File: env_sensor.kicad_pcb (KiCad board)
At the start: 2 copper layers, 147.9 x 143 mm, 56 parts, among them J1 E Paper, J10 PWMOUT, J11 Reg2, J12 I2C_Source, J13 I2C_2, J14 I2C_3, J15 MH-Z19, J16 ADCs, J17 Conn_01x04_Pin, J2 Reg1, J3 Barrel_Jack, J4 LED_OUTPUT, J5 Conn_01x04_Pin, J6 I2C_1, J6 I2c, J7 USB_C_Receptacle_USB2.0_16P, J9 DEBUG, Q1 NMOS, Q2 NMOS, Q3 NMOS, U1 MH-Z19B, U3 ESP32-S3-WROOM-1, U4 TXB0104PW, U6 TPS2065CDBV, U7 AP7361C-33E, Y1 Crystal

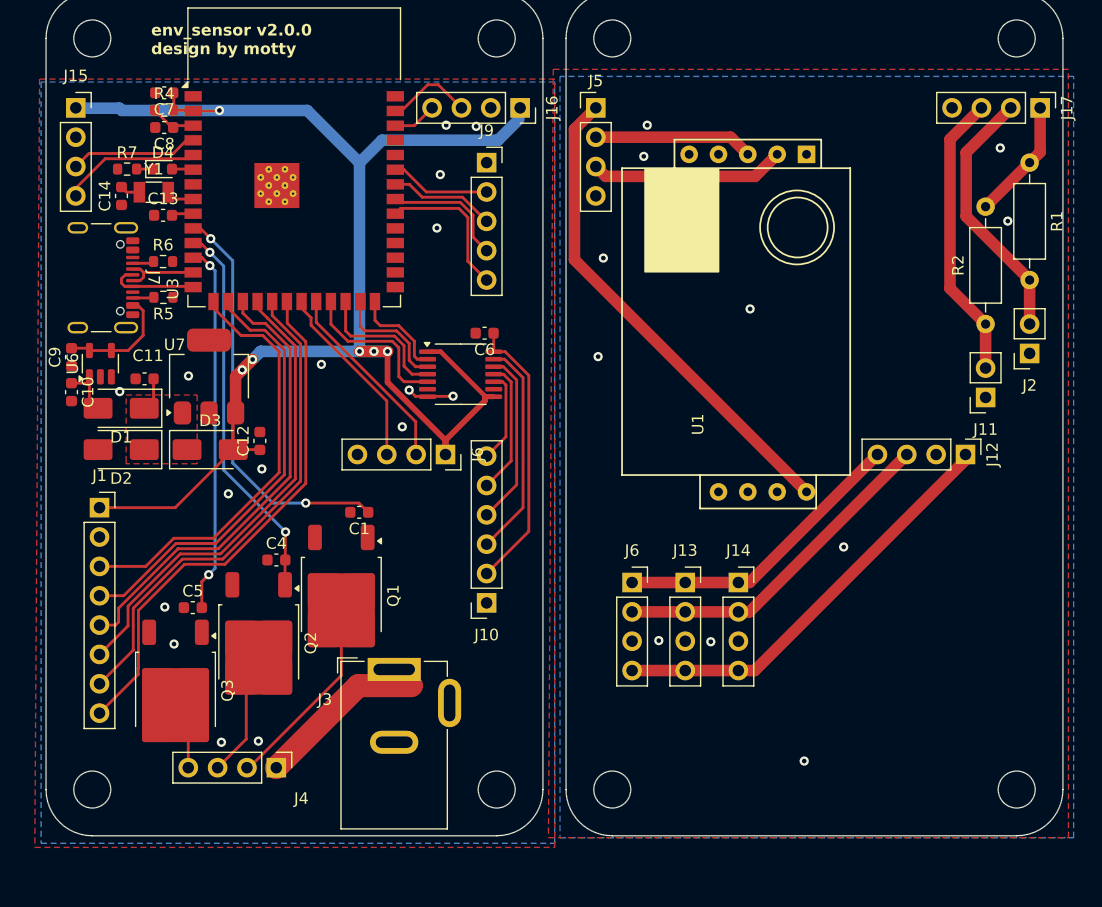
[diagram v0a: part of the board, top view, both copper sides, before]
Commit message: update lib for switch and fix DRCs
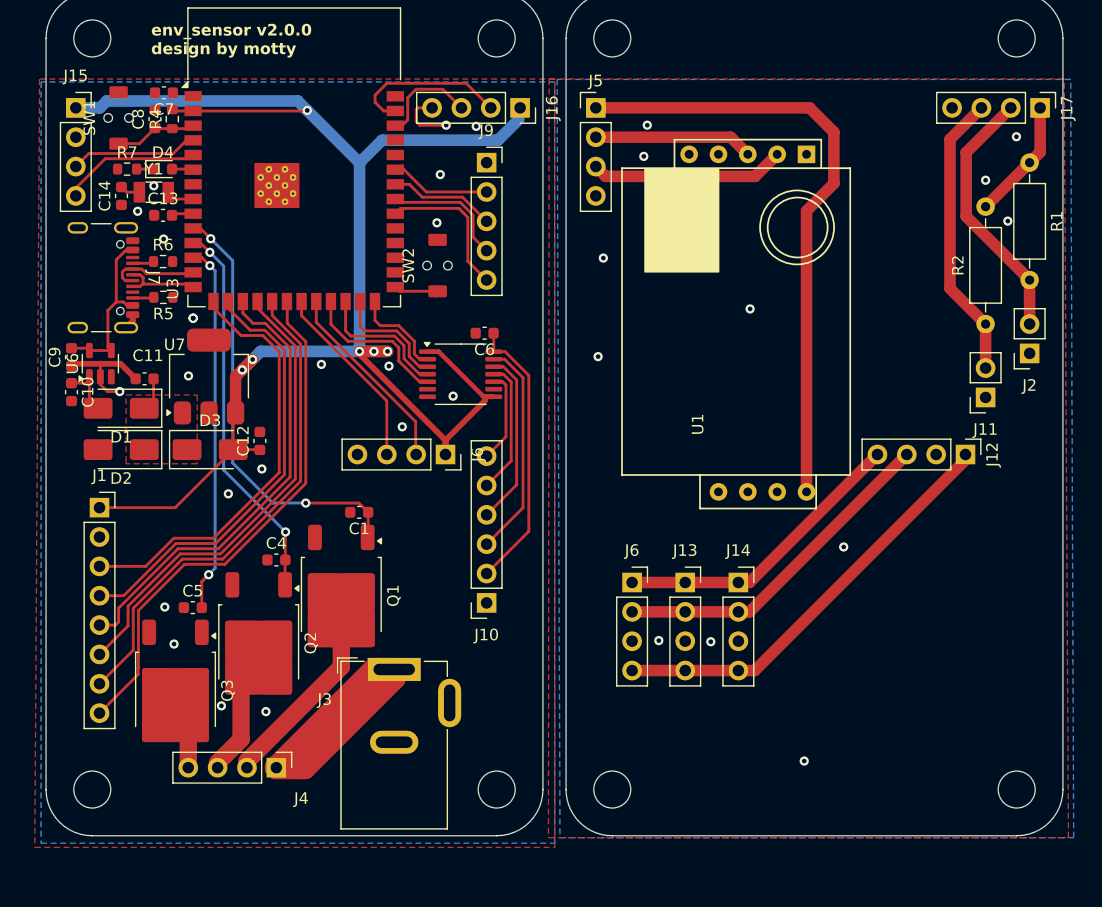
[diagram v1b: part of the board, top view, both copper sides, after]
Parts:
- added SW1: EN, paripalpp_button:TVAF06-A020B-R, F.Cu at (106.3, 51.9)
- added SW2: BOOT, paripalpp_button:TVAF06-A020B-R, F.Cu at (133.9, 64.7)
- moved C8 1.08 mm to (109.4, 52.0), turned to 90 degrees
- moved R4 1.04 mm to (110.9, 52.0), turned to 90 degrees
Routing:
- net v12: track 14.6 -> 27.9 mm
- net GND: track 3.93 -> 16.5 mm, vias 16 -> 21
- net /sensor/v5v: track 42.3 -> 53.6 mm
- net v3v: track 130.0 -> 137.6 mm
- net adc1: track 7.49 -> 14.5 mm
- net Net-(U6-EN): track 10.1 -> 15.1 mm
- net adc2: track 3.82 -> 8.82 mm
- net IO0: track 0.00 -> 4.79 mm
- net EN: track 4.01 -> 7.14 mm
- net LED_C1: track 35.6 -> 37.8 mm
- net IO19: track 6.82 -> 7.93 mm
- net AD3: track 13.8 -> 13.1 mm
- net LED_V2: track 11.0 -> 10.2 mm
- net /sensor/GND: vias 11 -> 12

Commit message: update
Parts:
- added J18: Conn_01x02_Pin, Connector_PinHeader_2.54mm:PinHeader_1x02_P2.54mm_Vertical, F.Cu at (138.1, 100.9)
- added J8: v5_v3, Connector_PinSocket_2.54mm:PinSocket_1x03_P2.54mm_Vertical, F.Cu at (132.9, 93.8)
- J12, J17, J5: moved to B.Cu
- J9: footprint Connector_PinSocket_2.54mm:PinSocket_1x05_P2.54mm_Vertical -> Connector_PinHeader_2.54mm:PinHeader_1x05_P2.54mm_Vertical
- moved J13 26.6 mm to (181.7, 88.7), turned to 180 degrees
- moved C6 21.7 mm to (135.6, 92.1), turned to -90 degrees
- moved J14 18.3 mm to (176.1, 100.7), turned to 90 degrees
- moved J12 11.7 mm to (172.0, 72.1), turned to 180 degrees
- moved J6 11.6 mm to (127.1, 72.1), turned to 0 degrees
- moved SW2 10.0 mm to (138.1, 73.7), turned to 0 degrees
- moved U4 9.83 mm to (131.9, 83.0), turned to -90 degrees
- moved J6 8.81 mm to (148.7, 100.7), turned to 90 degrees
- moved SW1 7.05 mm to (101.9, 57.4), turned to 0 degrees
- moved C8 5.24 mm to (104.6, 54.0)
- moved R4 5.23 mm to (106.1, 54.0)
- moved C7 5.02 mm to (107.6, 54.0), turned to -90 degrees
- moved J11 4.63 mm to (181.5, 71.4)
- moved R2 3.86 mm to (181.5, 65.9)
- moved J2 0.81 mm to (185.1, 71.4)
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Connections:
- net Net-(J10-Pin_2) renamed /VServo
- J15 pad 1: v3v -> VCC
- J15 pad 3: RX(ESP_DOWN) -> TX(ESP_UP)
- J15 pad 4: TX(ESP_UP) -> RX(ESP_DOWN)
- J5 pad 2: /sensor/UART(d2u) -> /sensor/GND
- J5 pad 3: /sensor/UART(u2d) -> /sensor/TX(ESP_DOWN)
- J5 pad 4: /sensor/GND -> /sensor/RX(ESP_UP)
- U1 pad 2: /sensor/UART(u2d) -> /sensor/RX(ESP_UP)
- U1 pad 3: /sensor/UART(d2u) -> /sensor/TX(ESP_DOWN)
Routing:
- net VCC: track 4.01 -> 79.4 mm, vias 0 -> 4
- net v5v: track 0.00 -> 69.2 mm
- net /sensor/SCL: track 29.4 -> 65.8 mm
- net /sensor/SDA: track 25.8 -> 61.1 mm
- net /sensor/v3v: track 36.9 -> 65.8 mm
- net /sensor/UART(u2d): track 16.8 -> 0.00 mm
- net /sensor/UART(d2u): track 13.8 -> 0.00 mm
- net /sensor/v5v: track 53.6 -> 40.8 mm
- net Net-(J10-Pin_3): track 18.9 -> 8.52 mm
- net /sensor/TX(ESP_DOWN): track 0.00 -> 10.1 mm
- net /sensor/RX(ESP_UP): track 0.00 -> 10.1 mm
- net EN: track 7.14 -> 15.5 mm, vias 0 -> 2
- net Net-(J10-Pin_4): track 15.2 -> 7.46 mm
- net SCL: track 17.0 -> 10.0 mm
- net /VServo: track 24.2 -> 17.2 mm
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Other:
- board text added: "VCC GND MOSI SCLK CS DC RST BL"
- board text added: "env_sensor v3.0.0 design by motty LazyStance"
- board text removed: "${REFERENCE}"
- board text removed: "env_sensor v2.0.0 design by motty"

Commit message: ok
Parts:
- J6: value I2c -> ADCs
- J7: footprint Connector_USB:USB_C_Receptacle_GCT_USB4105-xx-A_16P_TopMnt_Horizontal -> Connector_USB:USB_C_Receptacle_GCT_USB4085
- moved J18 39.0 mm to (104.6, 81.1)
- moved C12 8.21 mm to (113.8, 86.6)
- moved C11 4.20 mm to (112.7, 74.2), turned to 90 degrees
- moved U6 4.19 mm to (108.9, 73.6)
- moved J7 3.86 mm to (106.2, 62.7)
- moved D2 3.49 mm to (109.9, 81.1)
- moved C10 3.46 mm to (105.6, 74.8), turned to 180 degrees
- moved D1 3.44 mm to (109.9, 77.5)
- moved C9 3.36 mm to (105.6, 72.5), turned to 0 degrees
- moved J22 3.15 mm to (151.9, 100.6)
- moved U7 3.15 mm to (117.2, 74.9)
- moved D3 2.93 mm to (117.1, 81.1)
- renumbered J6 to J22
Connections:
- J15 pad 3: TX(ESP_UP) -> RX(ESP_DOWN)
- J15 pad 4: RX(ESP_DOWN) -> TX(ESP_UP)
- J6 pad 2: SCL -> GND
- J6 pad 3: SDA -> SCL
- J6 pad 4: GND -> SDA
- U3 pad 4: RX(ESP_DOWN) -> TX(ESP_UP)
- U3 pad 5: TX(ESP_UP) -> RX(ESP_DOWN)
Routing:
- net v5v: track 69.2 -> 3.33 mm
- net Net-(U6-EN): track 14.7 -> 27.1 mm
- net GND: track 13.4 -> 2.11 mm, vias 30 -> 31
- net Net-(J7-CC2): track 1.87 -> 10.5 mm, vias 0 -> 1
- net VCC: track 79.4 -> 73.4 mm
- net v3v: track 139.0 -> 133.6 mm
- net /sensor/SDA: track 61.1 -> 57.9 mm
- net /sensor/SCL: track 65.8 -> 62.7 mm
- net /sensor/v3v: track 65.8 -> 62.7 mm
- net SDA: track 11.4 -> 14.2 mm
- net TX(ESP_UP): track 7.89 -> 5.12 mm
- net RX(ESP_DOWN): track 5.12 -> 7.89 mm
- net SCL: track 10.0 -> 12.1 mm
- net IO20: track 10.1 -> 11.9 mm, vias 2 -> 1
- net SPI_SCLK: track 38.1 -> 39.8 mm
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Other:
- board text added: "3.3V GND"
- board text added: "3.3V GND SCL SDA"
- board text added: "ADC1_CH0 ADC1_CH1"
- board text added: "GND TMS TDI TD0 TCK"

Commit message: update
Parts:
- removed J13: I2C_2, Connector_PinSocket_2.54mm:PinSocket_1x04_P2.54mm_Vertical
- removed J14: I2C_3, Connector_PinSocket_2.54mm:PinSocket_1x04_P2.54mm_Vertical
- removed J22: I2C_1, Connector_PinSocket_2.54mm:PinSocket_1x04_P2.54mm_Vertical
- added ?: , , F.Cu at (160.2, 88.4)
- added ?: , , F.Cu at (157.6, 98.6)
- added ?: , , F.Cu at (152.5, 101.1)
- added ?: , , F.Cu at (183.0, 96.0)
- added ?: , , F.Cu at (185.6, 91.0)
- added ?: , , F.Cu at (150.0, 96.0)
- added ?: , , F.Cu at (175.4, 96.0)
- added ?: , , F.Cu at (183.0, 93.5)
- added ?: , , F.Cu at (160.2, 103.7)
- added ?: , , F.Cu at (155.1, 106.2)
- added ?: , , F.Cu at (155.1, 96.0)
- added ?: , , F.Cu at (167.8, 103.7)
- added ?: , , F.Cu at (152.5, 106.2)
- added ?: , , F.Cu at (167.8, 98.6)
- added ?: , , F.Cu at (170.3, 111.3)
- added ?: , , F.Cu at (175.4, 106.2)
- added ?: , , F.Cu at (165.2, 106.2)
- added ?: , , F.Cu at (183.0, 101.1)
- added ?: , , F.Cu at (170.3, 96.0)
- added ?: , , F.Cu at (177.9, 91.0)
- added ?: , , F.Cu at (150.0, 103.7)
- added ?: , , F.Cu at (177.9, 111.3)
- added ?: , , F.Cu at (185.6, 98.6)
- added ?: , , F.Cu at (162.7, 91.0)
- added ?: , , F.Cu at (172.8, 96.0)
- added ?: , , F.Cu at (172.8, 91.0)
- added ?: , , F.Cu at (180.5, 106.2)
- added ?: , , F.Cu at (147.4, 98.6)
- added ?: , , F.Cu at (155.1, 98.6)
- added ?: , , F.Cu at (162.7, 85.9)
- added ?: , , F.Cu at (180.5, 91.0)
- added ?: , , F.Cu at (185.6, 96.0)
- added ?: , , F.Cu at (170.3, 108.7)
- added ?: , , F.Cu at (167.8, 106.2)
- added ?: , , F.Cu at (162.7, 98.6)
- added ?: , , F.Cu at (180.5, 103.7)
- added ?: , , F.Cu at (165.2, 88.4)
- added ?: , , F.Cu at (160.2, 96.0)
- added ?: , , F.Cu at (177.9, 106.2)
- added ?: , , F.Cu at (162.7, 101.1)
- added ?: , , F.Cu at (165.2, 108.7)
- added ?: , , F.Cu at (183.0, 98.6)
- added ?: , , F.Cu at (170.3, 101.1)
- added ?: , , F.Cu at (177.9, 103.7)
- added ?: , , F.Cu at (150.0, 88.4)
- added ?: , , F.Cu at (183.0, 85.9)
- added ?: , , F.Cu at (162.7, 106.2)
- added ?: , , F.Cu at (155.1, 103.7)
- added ?: , , F.Cu at (183.0, 91.0)
- added ?: , , F.Cu at (157.6, 101.1)
- added ?: , , F.Cu at (150.0, 98.6)
- added ?: , , F.Cu at (162.7, 108.7)
- added ?: , , F.Cu at (167.8, 111.3)
- added ?: , , F.Cu at (155.1, 93.5)
- added ?: , , F.Cu at (162.7, 103.7)
- added ?: , , F.Cu at (175.4, 103.7)
- added ?: , , F.Cu at (167.8, 108.7)
- added ?: , , F.Cu at (147.4, 85.9)
- added ?: , , F.Cu at (180.5, 88.4)
- added ?: , , F.Cu at (185.6, 85.9)
- added ?: , , F.Cu at (165.2, 93.5)
- added ?: , , F.Cu at (170.3, 93.5)
- added ?: , , F.Cu at (177.9, 85.9)
- added ?: , , F.Cu at (152.5, 93.5)
- added ?: , , F.Cu at (155.1, 88.4)
- added ?: , , F.Cu at (167.8, 85.9)
- added ?: , , F.Cu at (160.2, 101.1)
- added ?: , , F.Cu at (177.9, 93.5)
- added ?: , , F.Cu at (165.2, 101.1)
- added ?: , , F.Cu at (165.2, 96.0)
- added ?: , , F.Cu at (150.0, 91.0)
- added ?: , , F.Cu at (175.4, 88.4)
- added ?: , , F.Cu at (147.4, 96.0)
- added ?: , , F.Cu at (160.2, 106.2)
- added ?: , , F.Cu at (147.4, 91.0)
- added ?: , , F.Cu at (157.6, 93.5)
- added ?: , , F.Cu at (183.0, 103.7)
- added ?: , , F.Cu at (170.3, 106.2)
- added ?: , , F.Cu at (152.5, 88.4)
- added ?: , , F.Cu at (167.8, 91.0)
- added ?: , , F.Cu at (157.6, 96.0)
- added ?: , , F.Cu at (175.4, 111.3)
- added ?: , , F.Cu at (155.1, 101.1)
- added ?: , , F.Cu at (175.4, 91.0)
- added ?: , , F.Cu at (170.3, 98.6)
- added ?: , , F.Cu at (160.2, 85.9)
- added ?: , , F.Cu at (177.9, 108.7)
- added ?: , , F.Cu at (172.8, 98.6)
- added ?: , , F.Cu at (167.8, 96.0)
- added ?: , , F.Cu at (175.4, 98.6)
- added ?: , , F.Cu at (152.5, 96.0)
- added ?: , , F.Cu at (172.8, 108.7)
- added ?: , , F.Cu at (177.9, 98.6)
- added ?: , , F.Cu at (172.8, 103.7)
- added ?: , , F.Cu at (170.3, 88.4)
- added ?: , , F.Cu at (162.7, 96.0)
- added ?: , , F.Cu at (165.2, 91.0)
- added ?: , , F.Cu at (155.1, 91.0)
- added ?: , , F.Cu at (185.6, 88.4)
- added ?: , , F.Cu at (172.8, 85.9)
- added ?: , , F.Cu at (185.6, 101.1)
- added ?: , , F.Cu at (157.6, 88.4)
- added ?: , , F.Cu at (185.6, 103.7)
- added ?: , , F.Cu at (165.2, 85.9)
- added ?: , , F.Cu at (157.6, 108.7)
- added ?: , , F.Cu at (183.0, 88.4)
- added ?: , , F.Cu at (162.7, 93.5)
- added ?: , , F.Cu at (167.8, 88.4)
- added ?: , , F.Cu at (180.5, 96.0)
- added ?: , , F.Cu at (150.0, 85.9)
- added ?: , , F.Cu at (152.5, 98.6)
- added ?: , , F.Cu at (175.4, 93.5)
- added ?: , , F.Cu at (175.4, 85.9)
- added ?: , , F.Cu at (157.6, 91.0)
- added ?: , , F.Cu at (155.1, 108.7)
- added ?: , , F.Cu at (160.2, 93.5)
- added ?: , , F.Cu at (177.9, 88.4)
- added ?: , , F.Cu at (180.5, 101.1)
- added ?: , , F.Cu at (165.2, 98.6)
- added ?: , , F.Cu at (165.2, 111.3)
- added ?: , , F.Cu at (147.4, 103.7)
- added ?: , , F.Cu at (180.5, 93.5)
- added ?: , , F.Cu at (172.8, 88.4)
- added ?: , , F.Cu at (172.8, 106.2)
- added ?: , , F.Cu at (152.5, 85.9)
- added ?: , , F.Cu at (150.0, 93.5)
- added ?: , , F.Cu at (170.3, 103.7)
- added ?: , , F.Cu at (160.2, 108.7)
- added ?: , , F.Cu at (170.3, 85.9)
- added ?: , , F.Cu at (185.6, 93.5)
- added ?: , , F.Cu at (175.4, 101.1)
- added ?: , , F.Cu at (152.5, 91.0)
- added ?: , , F.Cu at (165.2, 103.7)
- added ?: , , F.Cu at (160.2, 98.6)
- added ?: , , F.Cu at (157.6, 85.9)
- added ?: , , F.Cu at (150.0, 101.1)
- added ?: , , F.Cu at (167.8, 101.1)
- added ?: , , F.Cu at (180.5, 98.6)
- added ?: , , F.Cu at (155.1, 85.9)
- added ?: , , F.Cu at (175.4, 108.7)
- added ?: , , F.Cu at (172.8, 101.1)
- added ?: , , F.Cu at (157.6, 111.3)
- added ?: , , F.Cu at (157.6, 106.2)
- added ?: , , F.Cu at (157.6, 103.7)
- added ?: , , F.Cu at (167.8, 93.5)
- added ?: , , F.Cu at (160.2, 111.3)
- added ?: , , F.Cu at (162.7, 88.4)
- added ?: , , F.Cu at (177.9, 96.0)
- added ?: , , F.Cu at (147.4, 88.4)
- added ?: , , F.Cu at (147.4, 93.5)
- added ?: , , F.Cu at (160.2, 91.0)
- added ?: , , F.Cu at (147.4, 101.1)
- added ?: , , F.Cu at (152.5, 103.7)
- added ?: , , F.Cu at (177.9, 101.1)
- added ?: , , F.Cu at (170.3, 91.0)
- added ?: , , F.Cu at (155.1, 111.3)
- added ?: , , F.Cu at (172.8, 111.3)
- added ?: , , F.Cu at (180.5, 85.9)
- added ?: , , F.Cu at (162.7, 111.3)
- added ?: , , F.Cu at (172.8, 93.5)
- R1, R2: value 1k -> ~
- moved U1 4.55 mm to (147.4, 53.8)
- moved C12 2.10 mm to (114.1, 84.5)
- moved R5 1.81 mm to (109.9, 69.2)
- moved SW1 0.71 mm to (101.9, 56.7)
- moved C7 0.08 mm to (107.5, 54.0)
- moved R4 0.08 mm to (106.0, 54.0)
- moved C8 0.08 mm to (104.5, 54.0)
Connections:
- net Net-(U6-EN) renamed /U6_OUT
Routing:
- net /sensor/SCL: track 62.7 -> 0.00 mm
- net /sensor/v3v: track 62.7 -> 0.00 mm
- net /sensor/SDA: track 57.9 -> 0.00 mm
- net /U6_OUT: track 27.1 -> 15.1 mm
- net /sensor/RX(ESP_UP): track 10.1 -> 5.35 mm
- net /sensor/TX(ESP_DOWN): track 10.1 -> 5.35 mm
- net IO19: track 12.8 -> 8.71 mm, vias 2 -> 1
- net VCC: track 73.4 -> 70.1 mm, vias 4 -> 3
- net IO20: track 11.9 -> 8.78 mm
- net v3v: track 133.6 -> 130.6 mm, vias 7 -> 8
- net adc1: track 13.0 -> 10.4 mm, vias 1 -> 0
- net DEBUG_TCK: track 12.9 -> 10.3 mm
- net /sensor/v5v: track 40.8 -> 38.3 mm
- net Net-(J7-CC2): track 10.5 -> 8.91 mm
- net DEBUG_TDO: track 10.9 -> 9.75 mm
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- added copper zone on F.Cu, net /U6_OUT
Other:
- outline, holes or cut-outs redrawn
- board text removed: "3.3V GND SCL SDA"

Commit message: update
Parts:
- removed ? (x160): , 
- removed REF** (x8): MountingHole_3.2mm_M3, MountingHole:MountingHole_3.2mm_M3
- moved R6 2.63 mm to (108.1, 62.6), turned to 90 degrees
- moved J12 1.39 mm to (172.8, 73.2)
- moved J6 1.28 mm to (127.8, 73.1)
- moved U4 0.92 mm to (132.8, 83.0)
- moved R5 0.22 mm to (109.7, 69.3)
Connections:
- net IO19 renamed USB_D-
- net IO20 renamed USB_D+
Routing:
- net /U6_OUT: track 15.1 -> 19.5 mm
- net GND: track 2.13 -> 0.12 mm, vias 37 -> 32
- net LED_V3: track 5.87 -> 4.31 mm
- net LED_V2: track 10.2 -> 8.69 mm
- net SCL: track 12.1 -> 13.4 mm
- net USB_D+: track 8.78 -> 10.0 mm, vias 1 -> 0
- net SDA: track 14.2 -> 15.4 mm
- net Net-(J7-CC2): track 8.91 -> 9.98 mm
- net Net-(J7-CC1): track 3.34 -> 2.27 mm, vias 1 -> 0
- net Net-(J10-Pin_5): track 7.63 -> 6.66 mm
- net Net-(J10-Pin_6): track 9.25 -> 8.35 mm
- net Net-(J10-Pin_3): track 8.52 -> 7.70 mm
- net v3v: track 130.6 -> 129.8 mm
- net adc1: track 10.4 -> 9.68 mm
- net Net-(J10-Pin_4): track 7.46 -> 6.81 mm
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- added copper zone on F.Cu, net /VServo

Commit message: update
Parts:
- removed D4: POWER, LED_SMD:LED_0603_1608Metric
- removed J12: I2C_Source, Connector_PinHeader_2.54mm:PinHeader_1x04_P2.54mm_Vertical
- removed R7: 1k, Resistor_SMD:R_0603_1608Metric
- added ?: ThroughHole1x01_P2.54mm, env-sensor:ThroughHole1x01_P2.54mm, F.Cu at (177.9, 78.2)
- added ?: ThroughHole1x01_P2.54mm, env-sensor:ThroughHole1x01_P2.54mm, F.Cu at (150.0, 103.7)
- added ?: ThroughHole1x01_P2.54mm, env-sensor:ThroughHole1x01_P2.54mm, F.Cu at (167.8, 80.8)
- added ?: ThroughHole1x01_P2.54mm, env-sensor:ThroughHole1x01_P2.54mm, F.Cu at (162.7, 101.1)
- added ?: ThroughHole1x01_P2.54mm, env-sensor:ThroughHole1x01_P2.54mm, F.Cu at (180.5, 103.7)
- added ?: , , F.Cu at (155.1, 96.0)
- added ?: ThroughHole1x01_P2.54mm, env-sensor:ThroughHole1x01_P2.54mm, F.Cu at (167.8, 101.1)
- added ?: ThroughHole1x01_P2.54mm, env-sensor:ThroughHole1x01_P2.54mm, F.Cu at (157.6, 98.6)
- added ?: ThroughHole1x01_P2.54mm, env-sensor:ThroughHole1x01_P2.54mm, F.Cu at (177.9, 85.9)
- added ?: ThroughHole1x01_P2.54mm, env-sensor:ThroughHole1x01_P2.54mm, F.Cu at (165.2, 88.4)
- added ?: ThroughHole1x01_P2.54mm, env-sensor:ThroughHole1x01_P2.54mm, F.Cu at (185.6, 83.3)
- added ?: ThroughHole1x01_P2.54mm, env-sensor:ThroughHole1x01_P2.54mm, F.Cu at (155.1, 111.3)
- added ?: ThroughHole1x01_P2.54mm, env-sensor:ThroughHole1x01_P2.54mm, F.Cu at (175.4, 106.2)
- added ?: ThroughHole1x01_P2.54mm, env-sensor:ThroughHole1x01_P2.54mm, F.Cu at (162.7, 103.7)
- added ?: ThroughHole1x01_P2.54mm, env-sensor:ThroughHole1x01_P2.54mm, F.Cu at (150.0, 93.5)
- added ?: ThroughHole1x01_P2.54mm, env-sensor:ThroughHole1x01_P2.54mm, F.Cu at (175.4, 96.0)
- added ?: ThroughHole1x01_P2.54mm, env-sensor:ThroughHole1x01_P2.54mm, F.Cu at (150.0, 91.0)
- added ?: ThroughHole1x01_P2.54mm, env-sensor:ThroughHole1x01_P2.54mm, F.Cu at (180.5, 96.0)
- added ?: ThroughHole1x01_P2.54mm, env-sensor:ThroughHole1x01_P2.54mm, F.Cu at (152.5, 91.0)
- added ?: ThroughHole1x01_P2.54mm, env-sensor:ThroughHole1x01_P2.54mm, F.Cu at (177.9, 93.5)
- added ?: ThroughHole1x01_P2.54mm, env-sensor:ThroughHole1x01_P2.54mm, F.Cu at (170.3, 91.0)
- added ?: ThroughHole1x01_P2.54mm, env-sensor:ThroughHole1x01_P2.54mm, F.Cu at (185.6, 101.1)
- added ?: ThroughHole1x01_P2.54mm, env-sensor:ThroughHole1x01_P2.54mm, F.Cu at (170.3, 70.6)
- added ?: ThroughHole1x01_P2.54mm, env-sensor:ThroughHole1x01_P2.54mm, F.Cu at (147.4, 91.0)
- added ?: ThroughHole1x01_P2.54mm, env-sensor:ThroughHole1x01_P2.54mm, F.Cu at (167.8, 98.6)
- added ?: ThroughHole1x01_P2.54mm, env-sensor:ThroughHole1x01_P2.54mm, F.Cu at (165.2, 106.2)
- added ?: ThroughHole1x01_P2.54mm, env-sensor:ThroughHole1x01_P2.54mm, F.Cu at (183.0, 88.4)
- added ?: ThroughHole1x01_P2.54mm, env-sensor:ThroughHole1x01_P2.54mm, F.Cu at (183.0, 83.3)
- added ?: ThroughHole1x01_P2.54mm, env-sensor:ThroughHole1x01_P2.54mm, F.Cu at (172.8, 103.7)
- added ?: ThroughHole1x01_P2.54mm, env-sensor:ThroughHole1x01_P2.54mm, F.Cu at (152.5, 88.4)
- added ?: ThroughHole1x01_P2.54mm, env-sensor:ThroughHole1x01_P2.54mm, F.Cu at (165.2, 91.0)
- added ?: ThroughHole1x01_P2.54mm, env-sensor:ThroughHole1x01_P2.54mm, F.Cu at (172.8, 70.6)
- added ?: ThroughHole1x01_P2.54mm, env-sensor:ThroughHole1x01_P2.54mm, F.Cu at (180.5, 85.9)
- added ?: ThroughHole1x01_P2.54mm, env-sensor:ThroughHole1x01_P2.54mm, F.Cu at (147.4, 88.4)
- added ?: ThroughHole1x01_P2.54mm, env-sensor:ThroughHole1x01_P2.54mm, F.Cu at (175.4, 93.5)
- added ?: ThroughHole1x01_P2.54mm, env-sensor:ThroughHole1x01_P2.54mm, F.Cu at (183.0, 96.0)
- added ?: ThroughHole1x01_P2.54mm, env-sensor:ThroughHole1x01_P2.54mm, F.Cu at (160.2, 88.4)
- added ?: ThroughHole1x01_P2.54mm, env-sensor:ThroughHole1x01_P2.54mm, F.Cu at (172.8, 96.0)
- added ?: ThroughHole1x01_P2.54mm, env-sensor:ThroughHole1x01_P2.54mm, F.Cu at (167.8, 103.7)
- added ?: ThroughHole1x01_P2.54mm, env-sensor:ThroughHole1x01_P2.54mm, F.Cu at (152.5, 93.5)
- added ?: ThroughHole1x01_P2.54mm, env-sensor:ThroughHole1x01_P2.54mm, F.Cu at (147.4, 93.5)
- added ?: ThroughHole1x01_P2.54mm, env-sensor:ThroughHole1x01_P2.54mm, F.Cu at (172.8, 106.2)
- added ?: ThroughHole1x01_P2.54mm, env-sensor:ThroughHole1x01_P2.54mm, F.Cu at (172.8, 108.7)
- added ?: ThroughHole1x01_P2.54mm, env-sensor:ThroughHole1x01_P2.54mm, F.Cu at (183.0, 101.1)
- added ?: , , F.Cu at (155.1, 98.6)
- added ?: ThroughHole1x01_P2.54mm, env-sensor:ThroughHole1x01_P2.54mm, F.Cu at (165.2, 98.6)
- added ?: ThroughHole1x01_P2.54mm, env-sensor:ThroughHole1x01_P2.54mm, F.Cu at (167.8, 88.4)
- added ?: ThroughHole1x01_P2.54mm, env-sensor:ThroughHole1x01_P2.54mm, F.Cu at (170.3, 88.4)
- added ?: ThroughHole1x01_P2.54mm, env-sensor:ThroughHole1x01_P2.54mm, F.Cu at (170.3, 101.1)
- added ?: ThroughHole1x01_P2.54mm, env-sensor:ThroughHole1x01_P2.54mm, F.Cu at (167.8, 75.7)
- added ?: ThroughHole1x01_P2.54mm, env-sensor:ThroughHole1x01_P2.54mm, F.Cu at (157.6, 93.5)
- added ?: ThroughHole1x01_P2.54mm, env-sensor:ThroughHole1x01_P2.54mm, F.Cu at (183.0, 103.7)
- added ?: ThroughHole1x01_P2.54mm, env-sensor:ThroughHole1x01_P2.54mm, F.Cu at (170.3, 98.6)
- added ?: ThroughHole1x01_P2.54mm, env-sensor:ThroughHole1x01_P2.54mm, F.Cu at (165.2, 103.7)
- added ?: , , F.Cu at (155.1, 101.1)
- added ?: ThroughHole1x01_P2.54mm, env-sensor:ThroughHole1x01_P2.54mm, F.Cu at (170.3, 96.0)
- added ?: ThroughHole1x01_P2.54mm, env-sensor:ThroughHole1x01_P2.54mm, F.Cu at (180.5, 91.0)
- added ?: ThroughHole1x01_P2.54mm, env-sensor:ThroughHole1x01_P2.54mm, F.Cu at (160.2, 111.3)
- added ?: ThroughHole1x01_P2.54mm, env-sensor:ThroughHole1x01_P2.54mm, F.Cu at (172.8, 85.9)
- added ?: ThroughHole1x01_P2.54mm, env-sensor:ThroughHole1x01_P2.54mm, F.Cu at (157.6, 96.0)
- added ?: ThroughHole1x01_P2.54mm, env-sensor:ThroughHole1x01_P2.54mm, F.Cu at (167.8, 91.0)
- added ?: ThroughHole1x01_P2.54mm, env-sensor:ThroughHole1x01_P2.54mm, F.Cu at (177.9, 70.6)
- added ?: ThroughHole1x01_P2.54mm, env-sensor:ThroughHole1x01_P2.54mm, F.Cu at (162.7, 96.0)
- added ?: , , F.Cu at (155.1, 91.0)
- added ?: ThroughHole1x01_P2.54mm, env-sensor:ThroughHole1x01_P2.54mm, F.Cu at (185.6, 98.6)
- added ?: ThroughHole1x01_P2.54mm, env-sensor:ThroughHole1x01_P2.54mm, F.Cu at (167.8, 73.2)
- added ?: ThroughHole1x01_P2.54mm, env-sensor:ThroughHole1x01_P2.54mm, F.Cu at (160.2, 101.1)
- added ?: ThroughHole1x01_P2.54mm, env-sensor:ThroughHole1x01_P2.54mm, F.Cu at (150.0, 88.4)
- added ?: ThroughHole1x01_P2.54mm, env-sensor:ThroughHole1x01_P2.54mm, F.Cu at (175.4, 98.6)
- added ?: ThroughHole1x01_P2.54mm, env-sensor:ThroughHole1x01_P2.54mm, F.Cu at (147.4, 101.1)
- added ?: ThroughHole1x01_P2.54mm, env-sensor:ThroughHole1x01_P2.54mm, F.Cu at (170.3, 108.7)
- added ?: ThroughHole1x01_P2.54mm, env-sensor:ThroughHole1x01_P2.54mm, F.Cu at (160.2, 98.6)
- added ?: ThroughHole1x01_P2.54mm, env-sensor:ThroughHole1x01_P2.54mm, F.Cu at (160.2, 96.0)
- added ?: ThroughHole1x01_P2.54mm, env-sensor:ThroughHole1x01_P2.54mm, F.Cu at (162.7, 88.4)
- added ?: ThroughHole1x01_P2.54mm, env-sensor:ThroughHole1x01_P2.54mm, F.Cu at (172.8, 101.1)
- added ?: ThroughHole1x01_P2.54mm, env-sensor:ThroughHole1x01_P2.54mm, F.Cu at (185.6, 91.0)
- added ?: ThroughHole1x01_P2.54mm, env-sensor:ThroughHole1x01_P2.54mm, F.Cu at (177.9, 88.4)
- added ?: ThroughHole1x01_P2.54mm, env-sensor:ThroughHole1x01_P2.54mm, F.Cu at (185.6, 103.7)
- added ?: ThroughHole1x01_P2.54mm, env-sensor:ThroughHole1x01_P2.54mm, F.Cu at (172.8, 98.6)
- added ?: ThroughHole1x01_P2.54mm, env-sensor:ThroughHole1x01_P2.54mm, F.Cu at (147.4, 103.7)
- added ?: , , F.Cu at (162.7, 111.3)
- added ?: ThroughHole1x01_P2.54mm, env-sensor:ThroughHole1x01_P2.54mm, F.Cu at (175.4, 91.0)
- added ?: ThroughHole1x01_P2.54mm, env-sensor:ThroughHole1x01_P2.54mm, F.Cu at (185.6, 96.0)
- added ?: ThroughHole1x01_P2.54mm, env-sensor:ThroughHole1x01_P2.54mm, F.Cu at (167.8, 83.3)
- added ?: ThroughHole1x01_P2.54mm, env-sensor:ThroughHole1x01_P2.54mm, F.Cu at (157.6, 91.0)
- added ?: ThroughHole1x01_P2.54mm, env-sensor:ThroughHole1x01_P2.54mm, F.Cu at (177.9, 96.0)
- added ?: ThroughHole1x01_P2.54mm, env-sensor:ThroughHole1x01_P2.54mm, F.Cu at (177.9, 73.2)
- added ?: ThroughHole1x01_P2.54mm, env-sensor:ThroughHole1x01_P2.54mm, F.Cu at (185.6, 85.9)
- added ?: ThroughHole1x01_P2.54mm, env-sensor:ThroughHole1x01_P2.54mm, F.Cu at (147.4, 96.0)
- added ?: ThroughHole1x01_P2.54mm, env-sensor:ThroughHole1x01_P2.54mm, F.Cu at (175.4, 83.3)
- added ?: , , F.Cu at (155.1, 88.4)
- added ?: ThroughHole1x01_P2.54mm, env-sensor:ThroughHole1x01_P2.54mm, F.Cu at (177.9, 108.7)
- added ?: ThroughHole1x01_P2.54mm, env-sensor:ThroughHole1x01_P2.54mm, F.Cu at (165.2, 101.1)
- added ?: ThroughHole1x01_P2.54mm, env-sensor:ThroughHole1x01_P2.54mm, F.Cu at (147.4, 98.6)
- added ?: ThroughHole1x01_P2.54mm, env-sensor:ThroughHole1x01_P2.54mm, F.Cu at (172.8, 93.5)
- added ?: , , F.Cu at (162.7, 108.7)
- added ?: ThroughHole1x01_P2.54mm, env-sensor:ThroughHole1x01_P2.54mm, F.Cu at (175.4, 111.3)
- added ?: ThroughHole1x01_P2.54mm, env-sensor:ThroughHole1x01_P2.54mm, F.Cu at (165.2, 111.3)
- added ?: ThroughHole1x01_P2.54mm, env-sensor:ThroughHole1x01_P2.54mm, F.Cu at (180.5, 93.5)
- added ?: ThroughHole1x01_P2.54mm, env-sensor:ThroughHole1x01_P2.54mm, F.Cu at (150.0, 101.1)
- added ?: ThroughHole1x01_P2.54mm, env-sensor:ThroughHole1x01_P2.54mm, F.Cu at (157.6, 108.7)
- added ?: ThroughHole1x01_P2.54mm, env-sensor:ThroughHole1x01_P2.54mm, F.Cu at (175.4, 85.9)
- added ?: ThroughHole1x01_P2.54mm, env-sensor:ThroughHole1x01_P2.54mm, F.Cu at (157.6, 103.7)
- added ?: ThroughHole1x01_P2.54mm, env-sensor:ThroughHole1x01_P2.54mm, F.Cu at (180.5, 83.3)
- added ?: ThroughHole1x01_P2.54mm, env-sensor:ThroughHole1x01_P2.54mm, F.Cu at (177.9, 101.1)
- added ?: ThroughHole1x01_P2.54mm, env-sensor:ThroughHole1x01_P2.54mm, F.Cu at (167.8, 106.2)
- added ?: ThroughHole1x01_P2.54mm, env-sensor:ThroughHole1x01_P2.54mm, F.Cu at (162.7, 98.6)
- added ?: ThroughHole1x01_P2.54mm, env-sensor:ThroughHole1x01_P2.54mm, F.Cu at (175.4, 103.7)
- added ?: ThroughHole1x01_P2.54mm, env-sensor:ThroughHole1x01_P2.54mm, F.Cu at (170.3, 111.3)
- added ?: ThroughHole1x01_P2.54mm, env-sensor:ThroughHole1x01_P2.54mm, F.Cu at (165.2, 93.5)
- added ?: ThroughHole1x01_P2.54mm, env-sensor:ThroughHole1x01_P2.54mm, F.Cu at (183.0, 91.0)
- added ?: ThroughHole1x01_P2.54mm, env-sensor:ThroughHole1x01_P2.54mm, F.Cu at (152.5, 103.7)
- added ?: ThroughHole1x01_P2.54mm, env-sensor:ThroughHole1x01_P2.54mm, F.Cu at (157.6, 111.3)
- added ?: ThroughHole1x01_P2.54mm, env-sensor:ThroughHole1x01_P2.54mm, F.Cu at (150.0, 98.6)
- added ?: ThroughHole1x01_P2.54mm, env-sensor:ThroughHole1x01_P2.54mm, F.Cu at (175.4, 108.7)
- added ?: , , F.Cu at (155.1, 93.5)
- added ?: ThroughHole1x01_P2.54mm, env-sensor:ThroughHole1x01_P2.54mm, F.Cu at (170.3, 93.5)
- added ?: ThroughHole1x01_P2.54mm, env-sensor:ThroughHole1x01_P2.54mm, F.Cu at (167.8, 78.2)
- added ?: ThroughHole1x01_P2.54mm, env-sensor:ThroughHole1x01_P2.54mm, F.Cu at (170.3, 78.2)
- added ?: ThroughHole1x01_P2.54mm, env-sensor:ThroughHole1x01_P2.54mm, F.Cu at (160.2, 103.7)
- added ?: ThroughHole1x01_P2.54mm, env-sensor:ThroughHole1x01_P2.54mm, F.Cu at (167.8, 111.3)
- added ?: ThroughHole1x01_P2.54mm, env-sensor:ThroughHole1x01_P2.54mm, F.Cu at (165.2, 96.0)
- added ?: ThroughHole1x01_P2.54mm, env-sensor:ThroughHole1x01_P2.54mm, F.Cu at (183.0, 93.5)
- added ?: ThroughHole1x01_P2.54mm, env-sensor:ThroughHole1x01_P2.54mm, F.Cu at (165.2, 108.7)
- added ?: ThroughHole1x01_P2.54mm, env-sensor:ThroughHole1x01_P2.54mm, F.Cu at (170.3, 103.7)
- added ?: ThroughHole1x01_P2.54mm, env-sensor:ThroughHole1x01_P2.54mm, F.Cu at (177.9, 83.3)
- added ?: ThroughHole1x01_P2.54mm, env-sensor:ThroughHole1x01_P2.54mm, F.Cu at (175.4, 88.4)
- added ?: ThroughHole1x01_P2.54mm, env-sensor:ThroughHole1x01_P2.54mm, F.Cu at (160.2, 108.7)
- added ?: ThroughHole1x01_P2.54mm, env-sensor:ThroughHole1x01_P2.54mm, F.Cu at (185.6, 88.4)
- added ?: ThroughHole1x01_P2.54mm, env-sensor:ThroughHole1x01_P2.54mm, F.Cu at (167.8, 70.6)
- added ?: ThroughHole1x01_P2.54mm, env-sensor:ThroughHole1x01_P2.54mm, F.Cu at (155.1, 106.2)
- added ?: ThroughHole1x01_P2.54mm, env-sensor:ThroughHole1x01_P2.54mm, F.Cu at (167.8, 96.0)
- added ?: ThroughHole1x01_P2.54mm, env-sensor:ThroughHole1x01_P2.54mm, F.Cu at (162.7, 93.5)
- added ?: ThroughHole1x01_P2.54mm, env-sensor:ThroughHole1x01_P2.54mm, F.Cu at (180.5, 101.1)
- added ?: , , F.Cu at (162.7, 106.2)
- added ?: ThroughHole1x01_P2.54mm, env-sensor:ThroughHole1x01_P2.54mm, F.Cu at (157.6, 88.4)
- added ?: ThroughHole1x01_P2.54mm, env-sensor:ThroughHole1x01_P2.54mm, F.Cu at (160.2, 91.0)
- added ?: ThroughHole1x01_P2.54mm, env-sensor:ThroughHole1x01_P2.54mm, F.Cu at (180.5, 98.6)
- added ?: ThroughHole1x01_P2.54mm, env-sensor:ThroughHole1x01_P2.54mm, F.Cu at (170.3, 106.2)
- added ?: ThroughHole1x01_P2.54mm, env-sensor:ThroughHole1x01_P2.54mm, F.Cu at (172.8, 88.4)
- added ?: ThroughHole1x01_P2.54mm, env-sensor:ThroughHole1x01_P2.54mm, F.Cu at (172.8, 91.0)
- added ?: ThroughHole1x01_P2.54mm, env-sensor:ThroughHole1x01_P2.54mm, F.Cu at (180.5, 88.4)
- added ?: ThroughHole1x01_P2.54mm, env-sensor:ThroughHole1x01_P2.54mm, F.Cu at (152.5, 101.1)
- added ?: ThroughHole1x01_P2.54mm, env-sensor:ThroughHole1x01_P2.54mm, F.Cu at (170.3, 83.3)
- added ?: ThroughHole1x01_P2.54mm, env-sensor:ThroughHole1x01_P2.54mm, F.Cu at (150.0, 96.0)
- added ?: ThroughHole1x01_P2.54mm, env-sensor:ThroughHole1x01_P2.54mm, F.Cu at (172.8, 111.3)
- added ?: ThroughHole1x01_P2.54mm, env-sensor:ThroughHole1x01_P2.54mm, F.Cu at (170.3, 73.2)
- added ?: ThroughHole1x01_P2.54mm, env-sensor:ThroughHole1x01_P2.54mm, F.Cu at (155.1, 108.7)
- added ?: ThroughHole1x01_P2.54mm, env-sensor:ThroughHole1x01_P2.54mm, F.Cu at (160.2, 93.5)
- added ?: ThroughHole1x01_P2.54mm, env-sensor:ThroughHole1x01_P2.54mm, F.Cu at (177.9, 103.7)
- added ?: ThroughHole1x01_P2.54mm, env-sensor:ThroughHole1x01_P2.54mm, F.Cu at (152.5, 98.6)
- added ?: ThroughHole1x01_P2.54mm, env-sensor:ThroughHole1x01_P2.54mm, F.Cu at (177.9, 111.3)
- added ?: ThroughHole1x01_P2.54mm, env-sensor:ThroughHole1x01_P2.54mm, F.Cu at (152.5, 96.0)
- added ?: ThroughHole1x01_P2.54mm, env-sensor:ThroughHole1x01_P2.54mm, F.Cu at (170.3, 75.7)
- added ?: ThroughHole1x01_P2.54mm, env-sensor:ThroughHole1x01_P2.54mm, F.Cu at (183.0, 98.6)
- added ?: , , F.Cu at (155.1, 103.7)
- added ?: ThroughHole1x01_P2.54mm, env-sensor:ThroughHole1x01_P2.54mm, F.Cu at (167.8, 93.5)
- added ?: ThroughHole1x01_P2.54mm, env-sensor:ThroughHole1x01_P2.54mm, F.Cu at (157.6, 106.2)
- added ?: ThroughHole1x01_P2.54mm, env-sensor:ThroughHole1x01_P2.54mm, F.Cu at (185.6, 93.5)
- added ?: ThroughHole1x01_P2.54mm, env-sensor:ThroughHole1x01_P2.54mm, F.Cu at (177.9, 106.2)
- added ?: ThroughHole1x01_P2.54mm, env-sensor:ThroughHole1x01_P2.54mm, F.Cu at (167.8, 85.9)
- added ?: ThroughHole1x01_P2.54mm, env-sensor:ThroughHole1x01_P2.54mm, F.Cu at (157.6, 101.1)
- added ?: ThroughHole1x01_P2.54mm, env-sensor:ThroughHole1x01_P2.54mm, F.Cu at (175.4, 70.6)
- added ?: ThroughHole1x01_P2.54mm, env-sensor:ThroughHole1x01_P2.54mm, F.Cu at (177.9, 98.6)
- added ?: ThroughHole1x01_P2.54mm, env-sensor:ThroughHole1x01_P2.54mm, F.Cu at (162.7, 91.0)
- added ?: ThroughHole1x01_P2.54mm, env-sensor:ThroughHole1x01_P2.54mm, F.Cu at (183.0, 85.9)
- added ?: ThroughHole1x01_P2.54mm, env-sensor:ThroughHole1x01_P2.54mm, F.Cu at (177.9, 91.0)
- added ?: ThroughHole1x01_P2.54mm, env-sensor:ThroughHole1x01_P2.54mm, F.Cu at (175.4, 101.1)
- added ?: ThroughHole1x01_P2.54mm, env-sensor:ThroughHole1x01_P2.54mm, F.Cu at (177.9, 75.7)
- added ?: ThroughHole1x01_P2.54mm, env-sensor:ThroughHole1x01_P2.54mm, F.Cu at (160.2, 106.2)
- added ?: ThroughHole1x01_P2.54mm, env-sensor:ThroughHole1x01_P2.54mm, F.Cu at (170.3, 80.8)
- added ?: ThroughHole1x01_P2.54mm, env-sensor:ThroughHole1x01_P2.54mm, F.Cu at (167.8, 108.7)
- added ?: ThroughHole1x01_P2.54mm, env-sensor:ThroughHole1x01_P2.54mm, F.Cu at (177.9, 80.8)
- added ?: ThroughHole1x01_P2.54mm, env-sensor:ThroughHole1x01_P2.54mm, F.Cu at (170.3, 85.9)
- added ?: ThroughHole1x01_P2.54mm, env-sensor:ThroughHole1x01_P2.54mm, F.Cu at (172.8, 83.3)
- added D5: POWER, LED_SMD:LED_0603_1608Metric, F.Cu at (108.8, 56.3)
- added J13: Conn_01x03_Socket, Connector_PinHeader_2.54mm:PinHeader_1x03_P2.54mm_Vertical, F.Cu at (138.9, 55.5)
- added R3: 1k, Resistor_SMD:R_0603_1608Metric, F.Cu at (105.8, 56.3)
- added REF**: MountingHole_3.2mm_M3, MountingHole:MountingHole_3.2mm_M3, F.Cu at (149.0, 45.0)
- added REF**: MountingHole_3.2mm_M3, MountingHole:MountingHole_3.2mm_M3, F.Cu at (104.0, 110.0)
- added REF**: MountingHole_3.2mm_M3, MountingHole:MountingHole_3.2mm_M3, F.Cu at (139.0, 45.0)
- added REF**: MountingHole_3.2mm_M3, MountingHole:MountingHole_3.2mm_M3, F.Cu at (139.0, 110.0)
- added REF**: MountingHole_3.2mm_M3, MountingHole:MountingHole_3.2mm_M3, F.Cu at (184.0, 45.0)
- added REF**: MountingHole_3.2mm_M3, MountingHole:MountingHole_3.2mm_M3, F.Cu at (184.0, 110.0)
- added REF**: MountingHole_3.2mm_M3, MountingHole:MountingHole_3.2mm_M3, F.Cu at (149.0, 110.0)
- added REF**: MountingHole_3.2mm_M3, MountingHole:MountingHole_3.2mm_M3, F.Cu at (104.0, 45.0)
- J10: footprint Connector_PinSocket_2.54mm:PinSocket_1x06_P2.54mm_Vertical -> Connector_PinHeader_2.54mm:PinHeader_1x06_P2.54mm_Vertical
- J6: value ADCs -> Conn_01x08_Socket; footprint Connector_PinSocket_2.54mm:PinSocket_1x04_P2.54mm_Vertical -> Connector_PinSocket_2.54mm:PinSocket_2x04_P2.54mm_Vertical
- J8: value v5_v3 -> Conn_01x08_Pin; footprint Connector_PinSocket_2.54mm:PinSocket_1x03_P2.54mm_Vertical -> Connector_PinHeader_2.54mm:PinHeader_2x04_P2.54mm_Vertical
- moved J8 45.0 mm to (172.8, 73.2), turned to 0 degrees
- moved J9 8.56 mm to (138.9, 64.3)
- moved C6 7.93 mm to (137.2, 84.3), turned to 0 degrees
- moved J10 7.88 mm to (140.9, 86.5), turned to 0 degrees
- moved SW2 6.17 mm to (139.0, 79.8)
- moved R5 3.28 mm to (113.0, 69.7)
- moved J7 2.88 mm to (109.0, 63.3)
- moved R6 2.67 mm to (107.0, 60.2), turned to 180 degrees
- moved C13 0.11 mm to (110.1, 60.2)
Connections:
- C6 pad 1: /VServo -> VCC
- J10 pad 2: /VServo -> VCC
- J6 pad 2: GND -> IO38
- J6 pad 3: SCL -> IO13
- J6 pad 4: SDA -> IO14
- J8 pad 1: VCC -> /sensor/v3v
- J8 pad 2: /VServo -> /sensor/IO38
- J8 pad 3: v3v -> /sensor/IO13
- U3 pad 21: SDA -> IO13
- U3 pad 22: SCL -> IO14
- U3 pad 31: unconnected-(U3-IO38-Pad31) -> IO38
- U3 pad 36: unconnected-(U3-RXD0-Pad36) -> Net-(J13-Pin_2)
- U3 pad 37: unconnected-(U3-TXD0-Pad37) -> Net-(J13-Pin_1)
- U3 pad 7: unconnected-(U3-IO7-Pad7) -> IO7
- U4 pad 14: /VServo -> VCC
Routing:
- net IO6: track 1.77 -> 30.4 mm, vias 0 -> 2
- net IO7: track 0.00 -> 27.1 mm, vias 0 -> 2
- net IO14: track 0.00 -> 18.1 mm
- net /VServo: track 17.8 -> 0.00 mm
- net IO38: track 0.00 -> 15.6 mm, vias 0 -> 1
- net SDA: track 15.4 -> 0.00 mm
- net IO13: track 0.00 -> 14.5 mm
- net SCL: track 13.4 -> 0.00 mm
- net VCC: track 69.6 -> 82.1 mm, vias 3 -> 4
- net Net-(J13-Pin_2): track 0.00 -> 9.92 mm
- net Net-(J13-Pin_1): track 0.00 -> 9.39 mm
- net Net-(J10-Pin_6): track 8.35 -> 16.9 mm
- net Net-(J10-Pin_5): track 6.66 -> 15.1 mm
- net DEBUG_TCK: track 10.3 -> 18.2 mm
- net DEBUG_TDO: track 9.75 -> 17.5 mm
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- removed copper zone on F.Cu, net /VServo
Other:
- board size 147.9 x 143 mm -> 88 x 73 mm
- board text added: "3.3V|IO38 IO13|IO14 IO6 | IO7 GND | GND"
- board text added: "5V in GND"
- board text added: "TX RX GND"
- board text removed: "3.3V GND"

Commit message: update
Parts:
- moved J10 2.05 mm to (138.9, 86.5)
- moved C6 0.41 mm to (137.1, 83.9)
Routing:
- net Net-(J10-Pin_4): track 13.1 -> 10.8 mm
- net Net-(J10-Pin_3): track 11.2 -> 9.14 mm
- net VCC: track 82.1 -> 80.2 mm
- net Net-(J10-Pin_5): track 15.1 -> 13.3 mm
- net Net-(J10-Pin_6): track 16.9 -> 16.1 mm
- net GND: vias 27 -> 30
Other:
- board text added: "TX -> RX <- GND"
- board text removed: "TX RX GND"
